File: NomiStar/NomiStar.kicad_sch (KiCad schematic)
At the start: 0 parts

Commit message: Sketched out the basic circuit without passives, LDO and LEDs (those will be on a separate board)
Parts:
- added J1, J2, J3, J4, J5: PINHD_1x4_Female, Connector_PinSocket_2.54mm:PinSocket_1x04_P2.54mm_Vertical, symbol PCM_SL_Pin_Headers:PINHD_1x4_Female
- added J6: Micro_SD_Card_Det1, symbol Connector:Micro_SD_Card_Det1
- added J7: USB_C_Receptacle_USB2.0_16P, symbol Connector:USB_C_Receptacle_USB2.0_16P
- added R1, R2: 5.1 k, PCM_Resistor_SMD_AKL:R_0603_1608Metric, symbol PCM_Resistor_AKL:R_0603
- added R6, R7, R8: 10 k, PCM_Resistor_SMD_AKL:R_0603_1608Metric, symbol PCM_Resistor_AKL:R_0603
- added U1: STM32F373CBTx, Package_QFP:LQFP-48_7x7mm_P0.5mm, symbol MCU_ST_STM32F3:STM32F373CBTx
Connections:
- new net: J7.A5 (CC1), R1.2
- new net: J7.B5 (CC2), R2.2
- new net: J6.1 (DAT2), R7.1
- new net: J4.2, U1.13 (PA3)
- new net: J5.2, U1.29 (PA8)
- new net: J1.2, U1.10 (PA0)
- new net: J2.2, U1.11 (PA1)
- new net: J3.2, U1.12 (PA2)
- new net: J6.2 (DAT3/CD), R6.2, U1.14 (PA4)
- new net: J6.5 (CLK), U1.15 (PA5)
- new net: J6.7 (DAT0), U1.16 (PA6)
- new net: J6.3 (CMD), U1.18 (PB0)
- new net: J6.9 (DET), U1.27 (PB15)
- new net: J7.A7 (D-), J7.B7 (D-), U1.32 (PA11)
- new net: J7.A6 (D+), J7.B6 (D+), U1.33 (PA12)
- new net: J6.8 (DAT1), R8.1
- new net +3.3V: J1.3, J2.3, J3.3, J4.3, J5.3, J6.4 (VDD), R6.1, R7.2, R8.2, U1.1 (VBAT), U1.17 (VDD), U1.48 (VDD), U1.9 (VDDA)
- new net +5V: J7.A4 (VBUS), J7.A9 (VBUS), J7.B4 (VBUS), J7.B9 (VBUS)
- new net GND: J1.1, J1.4, J2.1, J2.4, J3.1, J3.4, J4.1, J4.4, J5.1, J5.4, J6.6 (VSS), J6.SH (SHIELD), J7.A1 (GND), J7.A12 (GND), J7.B1 (GND), J7.B12 (GND), J7.SH (SHIELD), R1.1, R2.1, U1.47 (VSS), U1.8 (VSSA)

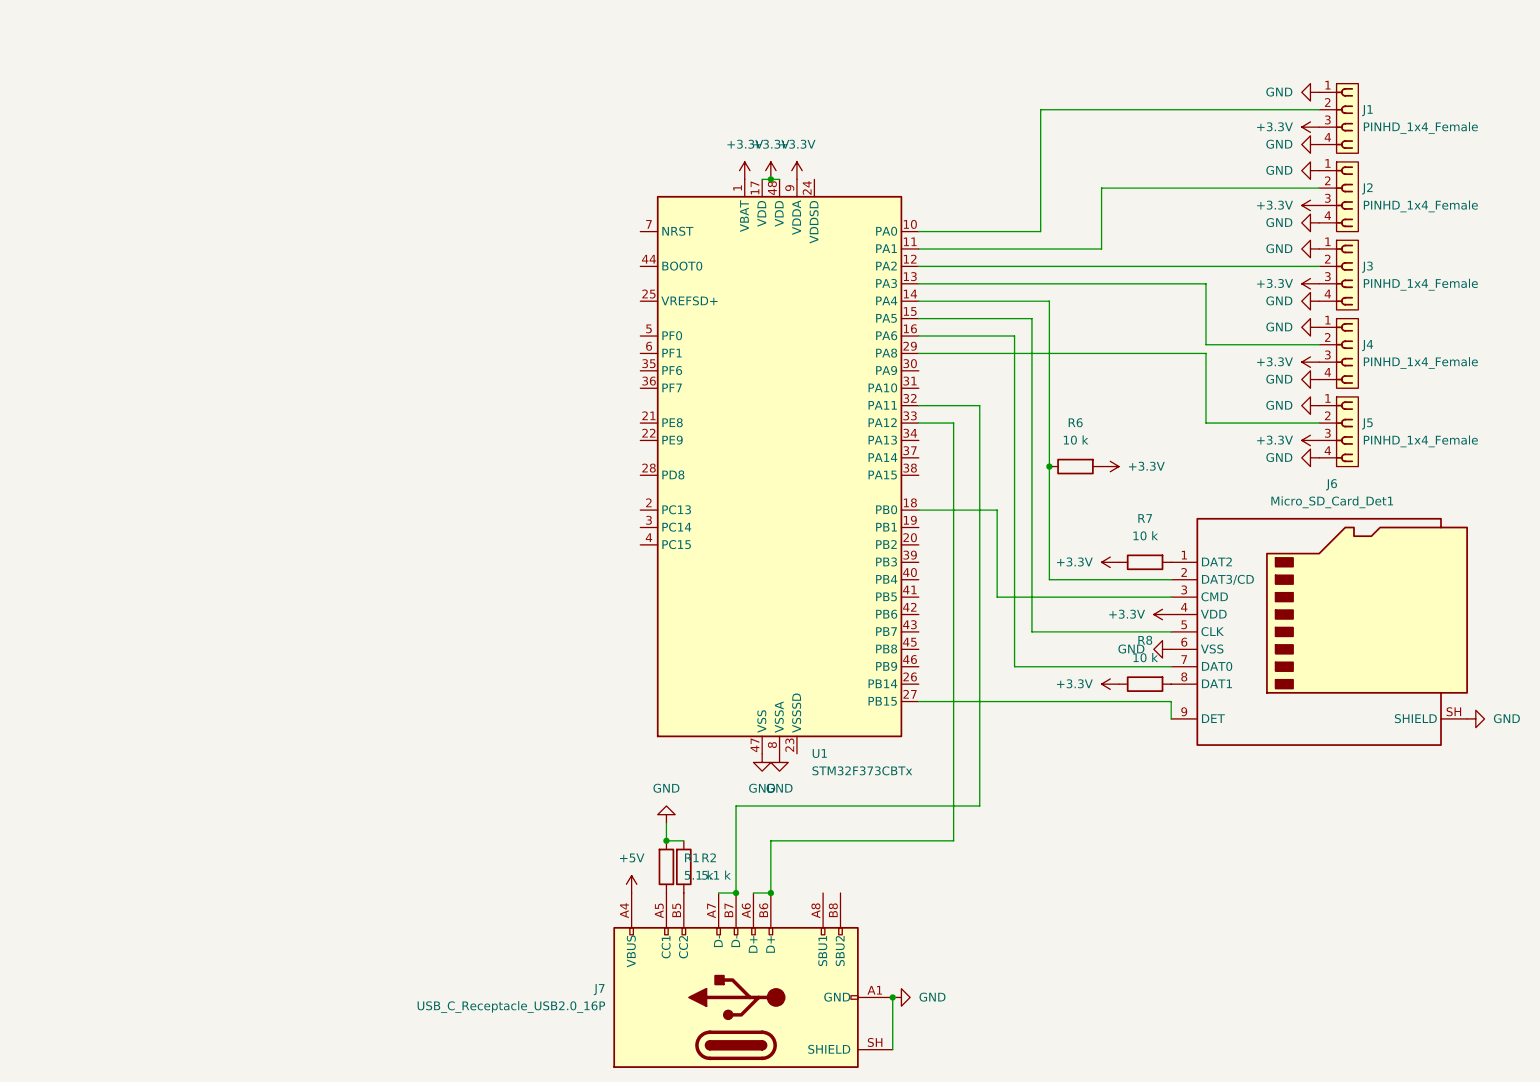
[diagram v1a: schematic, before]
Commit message: Working on finishing the main board, not yet started on the star points
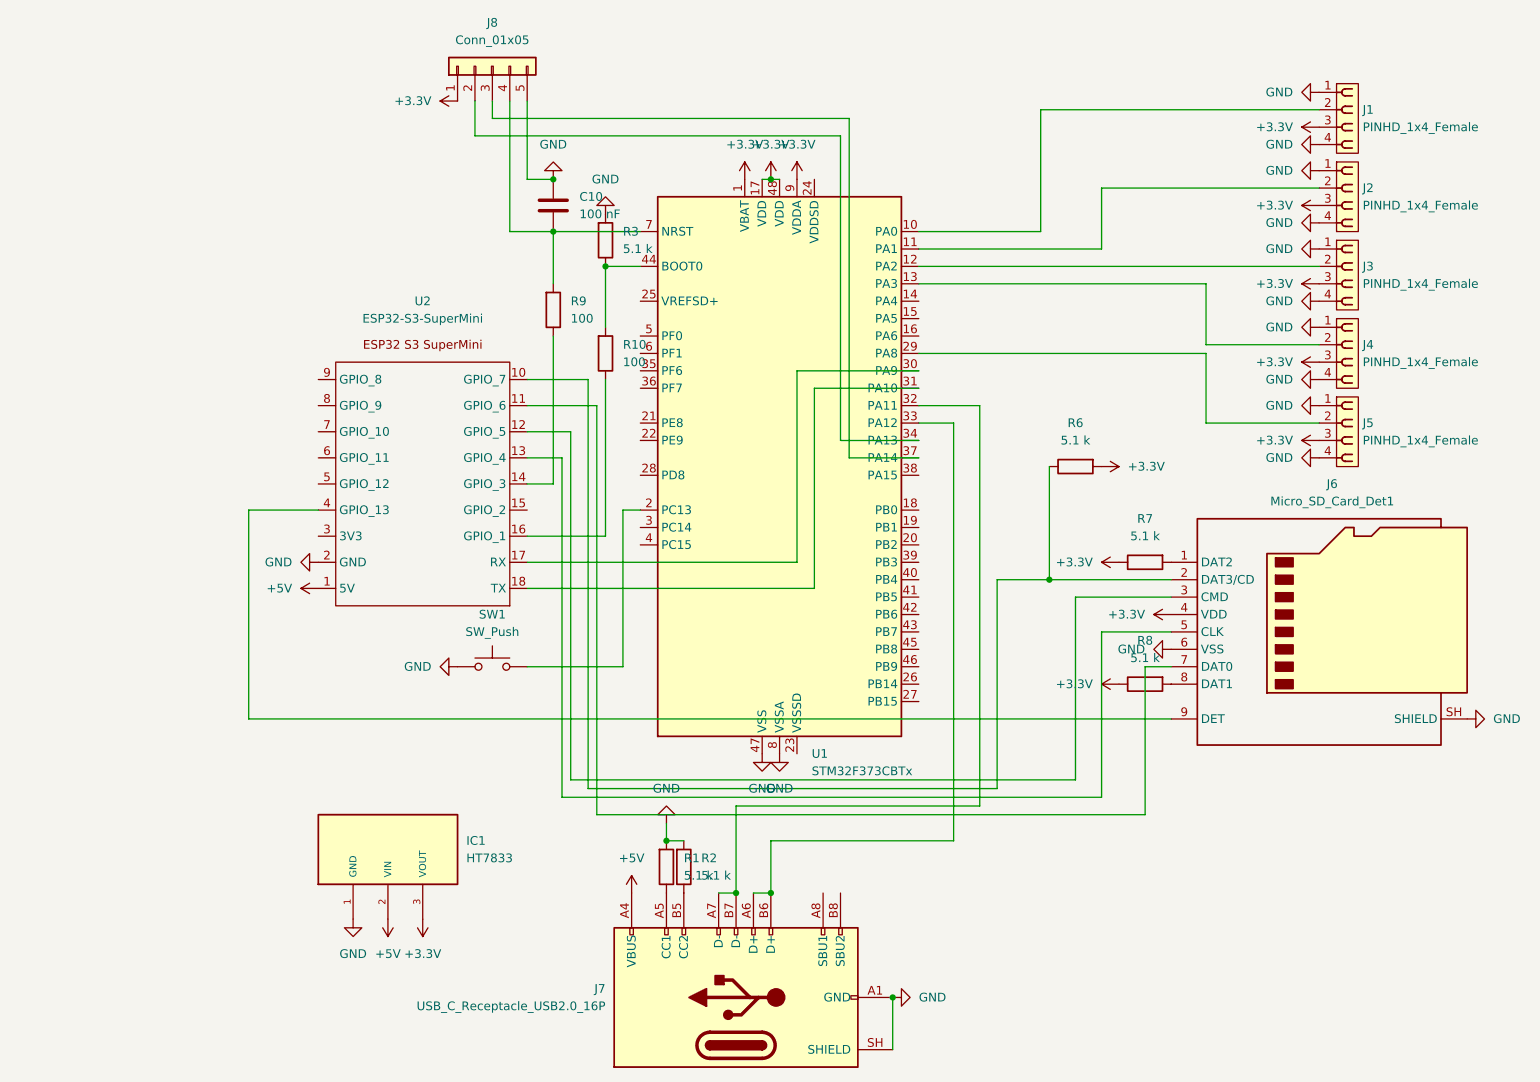
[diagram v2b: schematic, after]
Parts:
- added C10: 100 nF, symbol Device:C
- added IC1: HT7833, HT7833:HT7833, symbol HT7833:HT7833
- added J8: Conn_01x05, Connector_PinHeader_1.27mm:PinHeader_1x05_P1.27mm_Vertical, symbol Connector_Generic:Conn_01x05
- added R10, R9: 100, PCM_Resistor_SMD_AKL:R_0603_1608Metric, symbol PCM_Resistor_AKL:R_0603
- added R3: 5.1 k, PCM_Resistor_SMD_AKL:R_0603_1608Metric, symbol PCM_Resistor_AKL:R_0603
- added SW1: SW_Push, Button_Switch_SMD:SW_Push_SPST_NO_Alps_SKRK, symbol Switch:SW_Push
- added U2: ESP32-S3-SuperMini, ESP-super_mini:ESP32-S3-SuperMini, symbol ESP-SuperMini:ESP32-S3-SuperMini
- J6: footprint (none) -> Connector_Card:microSD_HC_Molex_104031-0811
- R1: footprint PCM_Resistor_SMD_AKL:R_0603_1608Metric -> Resistor_SMD:R_0603_1608Metric
- R6, R7, R8: value 10 k -> 5.1 k
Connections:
- net +3.3V: now also IC1.3 (VOUT), J8.1 (Pin_1)
- net +5V: now also IC1.2 (VIN), IC1.2@1 (VIN), U2.1 (5V)
- net GND: now also C10.1, IC1.1 (GND), J8.5 (Pin_5), R3.1, SW1.1, U2.2 (GND)
- net at J6.2 (DAT3/CD), R6.2: now also U2.10 (GPIO_7); no longer U1.14 (PA4)
- net at U1.15 (PA5): no longer J6.5 (CLK)
- net at U1.16 (PA6): no longer J6.7 (DAT0)
- net at U1.18 (PB0): no longer J6.3 (CMD)
- net at U1.2 (PC13): now also SW1.2
- net at U1.27 (PB15): no longer J6.9 (DET)
- net at U1.30 (PA9): now also U2.17 (RX)
- net at U1.31 (PA10): now also U2.18 (TX)
- net at U1.34 (PA13): now also J8.2 (Pin_2)
- net at U1.37 (PA14): now also J8.3 (Pin_3)
- net at U1.44 (BOOT0): now also R10.1, R3.2
- net at U1.7 (NRST): now also C10.2, J8.4 (Pin_4), R9.1
- new net: J6.7 (DAT0), U2.11 (GPIO_6)
- new net: J6.3 (CMD), U2.12 (GPIO_5)
- new net: J6.5 (CLK), U2.13 (GPIO_4)
- new net: R9.2, U2.14 (GPIO_3)
- new net: R10.2, U2.16 (GPIO_1)
- new net: J6.9 (DET), U2.4 (GPIO_13)

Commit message: Finished the pentagon board Need to design and draw up the point boards, maybe panelize it myself into small 2 boards
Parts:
- removed U2: ESP32-S3-SuperMini, ESP-super_mini:ESP32-S3-SuperMini, symbol ESP-SuperMini:ESP32-S3-SuperMini
- added U3: ESP32-C3_SUPERMINI_TH, ESP-super_mini:MODULE_ESP32-C3_SUPERMINI_TH, symbol ESP32-C3_SUPERMINI_TH:ESP32-C3_SUPERMINI_TH
- C10: footprint (none) -> Capacitor_SMD:C_0603_1608Metric
- J7: footprint (none) -> Connector_USB:USB_C_Receptacle_GCT_USB4105-xx-A_16P_TopMnt_Horizontal
- J8: footprint Connector_PinHeader_1.27mm:PinHeader_1x05_P1.27mm_Vertical -> Connector_PinHeader_2.54mm:PinHeader_1x05_P2.54mm_Vertical
- R10, R2, R3, R6, R7, R8, R9: footprint PCM_Resistor_SMD_AKL:R_0603_1608Metric -> Resistor_SMD:R_0603_1608Metric
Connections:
- net +5V: now also U3.5V
- net GND: now also U3.G (GND)
- net at U1.30 (PA9): now also U3.20 (GPIO20)
- net at U1.31 (PA10): now also U3.21 (GPIO21)
- net at J6.2 (DAT3/CD), R6.2: now also U3.7 (GPIO7)
- net at J6.7 (DAT0): now also U3.6 (GPIO6)
- net at J6.3 (CMD): now also U3.5 (GPIO5)
- net at J6.5 (CLK): now also U3.4 (GPIO4)
- net at R9.2: now also U3.3 (GPIO3)
- net at R10.2: now also U3.1 (GPIO1)
- net at J6.9 (DET): now also U3.10 (GPIO10)

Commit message: Finished the center PCB, will move onto the point schematic and PCB next
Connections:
- net +3.3V: no longer J1.3, J2.3, J3.3, J4.3, J5.3
- net +5V: now also J1.3, J2.3, J3.3, J4.3, J5.3
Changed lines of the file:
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@@
 	)
 	(symbol
-		(lib_id "power:+3.3V")
+		(lib_id "power:+5V")
 		(at 214.63 71.12 90)
 		(unit 1)
@@
 		(in_pos_files yes)
 		(dnp no)
-		(fields_autoplaced yes)
 		(property "Reference" "#PWR017"
 			(at 218.44 71.12 0)
@@
 			)
 		)
-		(property "Value" "+3.3V"
-			(at 210.82 71.1199 90)
-			(show_name no)
-			(do_not_autoplace no)
-			(effects
-				(font
-					(size 1.27 1.27)
-				)
-				(justify left)
+		(property "Value" "+5V"
+			(at 208.28 71.12 90)
+			(show_name no)
+			(do_not_autoplace no)
+			(effects
+				(font
+					(size 1.27 1.27)
+				)
 			)
 		)
@@
 			)
 		)
-		(property "Description" "Power symbol creates a global label with name \"+3.3V\""
+		(property "Description" "Power symbol creates a global label with name \"+5V\""
 			(at 214.63 71.12 0)
 			(hide yes)
@@
 	)
 	(symbol
-		(lib_id "power:+3.3V")
+		(lib_id "power:+5V")
 		(at 214.63 82.55 90)
 		(unit 1)
@@
 		(in_pos_files yes)
 		(dnp no)
-		(fields_autoplaced yes)
 		(property "Reference" "#PWR018"
 			(at 218.44 82.55 0)
@@
 			)
 		)
-		(property "Value" "+3.3V"
-			(at 210.82 82.5499 90)
-			(show_name no)
-			(do_not_autoplace no)
-			(effects
-				(font
-					(size 1.27 1.27)
-				)
-				(justify left)
+		(property "Value" "+5V"
+			(at 208.28 82.55 90)
+			(show_name no)
+			(do_not_autoplace no)
+			(effects
+				(font
+					(size 1.27 1.27)
+				)
 			)
 		)
@@
 			)
 		)
-		(property "Description" "Power symbol creates a global label with name \"+3.3V\""
+		(property "Description" "Power symbol creates a global label with name \"+5V\""
 			(at 214.63 82.55 0)
 			(hide yes)
@@
 	)
 	(symbol
-		(lib_id "power:+3.3V")
+		(lib_id "power:+5V")
 		(at 214.63 59.69 90)
 		(unit 1)
@@
 		(in_pos_files yes)
 		(dnp no)
-		(fields_autoplaced yes)
 		(property "Reference" "#PWR016"
 			(at 218.44 59.69 0)
@@
 			)
 		)
-		(property "Value" "+3.3V"
-			(at 210.82 59.6899 90)
-			(show_name no)
-			(do_not_autoplace no)
-			(effects
-				(font
-					(size 1.27 1.27)
-				)
-				(justify left)
+		(property "Value" "+5V"
+			(at 208.534 59.69 90)
+			(show_name no)
+			(do_not_autoplace no)
+			(effects
+				(font
+					(size 1.27 1.27)
+				)
 			)
 		)
@@
 			)
 		)
-		(property "Description" "Power symbol creates a global label with name \"+3.3V\""
+		(property "Description" "Power symbol creates a global label with name \"+5V\""
 			(at 214.63 59.69 0)
 			(hide yes)
@@
 	)
 	(symbol
-		(lib_id "power:+3.3V")
+		(lib_id "power:+5V")
 		(at 214.63 48.26 90)
 		(unit 1)
@@
 		(in_pos_files yes)
 		(dnp no)
-		(fields_autoplaced yes)
 		(property "Reference" "#PWR015"
 			(at 218.44 48.26 0)
@@
 			)
 		)
-		(property "Value" "+3.3V"
-			(at 210.82 48.2599 90)
-			(show_name no)
-			(do_not_autoplace no)
-			(effects
-				(font
-					(size 1.27 1.27)
-				)
-				(justify left)
+		(property "Value" "+5V"
+			(at 208.534 48.26 90)
+			(show_name no)
+			(do_not_autoplace no)
+			(effects
+				(font
+					(size 1.27 1.27)
+				)
 			)
 		)
@@
 			)
 		)
-		(property "Description" "Power symbol creates a global label with name \"+3.3V\""
+		(property "Description" "Power symbol creates a global label with name \"+5V\""
 			(at 214.63 48.26 0)
 			(hide yes)
@@
 	)
 	(symbol
-		(lib_id "power:+3.3V")
+		(lib_id "power:+5V")
 		(at 214.63 36.83 90)
 		(unit 1)
@@
 		(in_pos_files yes)
 		(dnp no)
-		(fields_autoplaced yes)
 		(property "Reference" "#PWR014"
 			(at 218.44 36.83 0)
@@
 			)
 		)
-		(property "Value" "+3.3V"
-			(at 210.82 36.8299 90)
-			(show_name no)
-			(do_not_autoplace no)
-			(effects
-				(font
-					(size 1.27 1.27)
-				)
-				(justify left)
+		(property "Value" "+5V"
+			(at 208.788 36.83 90)
+			(show_name no)
+			(do_not_autoplace no)
+			(effects
+				(font
+					(size 1.27 1.27)
+				)
 			)
 		)
@@
 			)
 		)
-		(property "Description" "Power symbol creates a global label with name \"+3.3V\""
+		(property "Description" "Power symbol creates a global label with name \"+5V\""
 			(at 214.63 36.83 0)
 			(hide yes)
